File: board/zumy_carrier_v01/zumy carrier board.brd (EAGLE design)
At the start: 54 x 88.9 mm, 20 parts, among them J1 ODROID_POWER, J2 BATT_POWER, M1 POLOLU_STEP_DOWN, M2 ITG/MPU_MODULE, M3 POLOLU_DRV8833_MODULE, SW1 500SSP1S1M6QEA

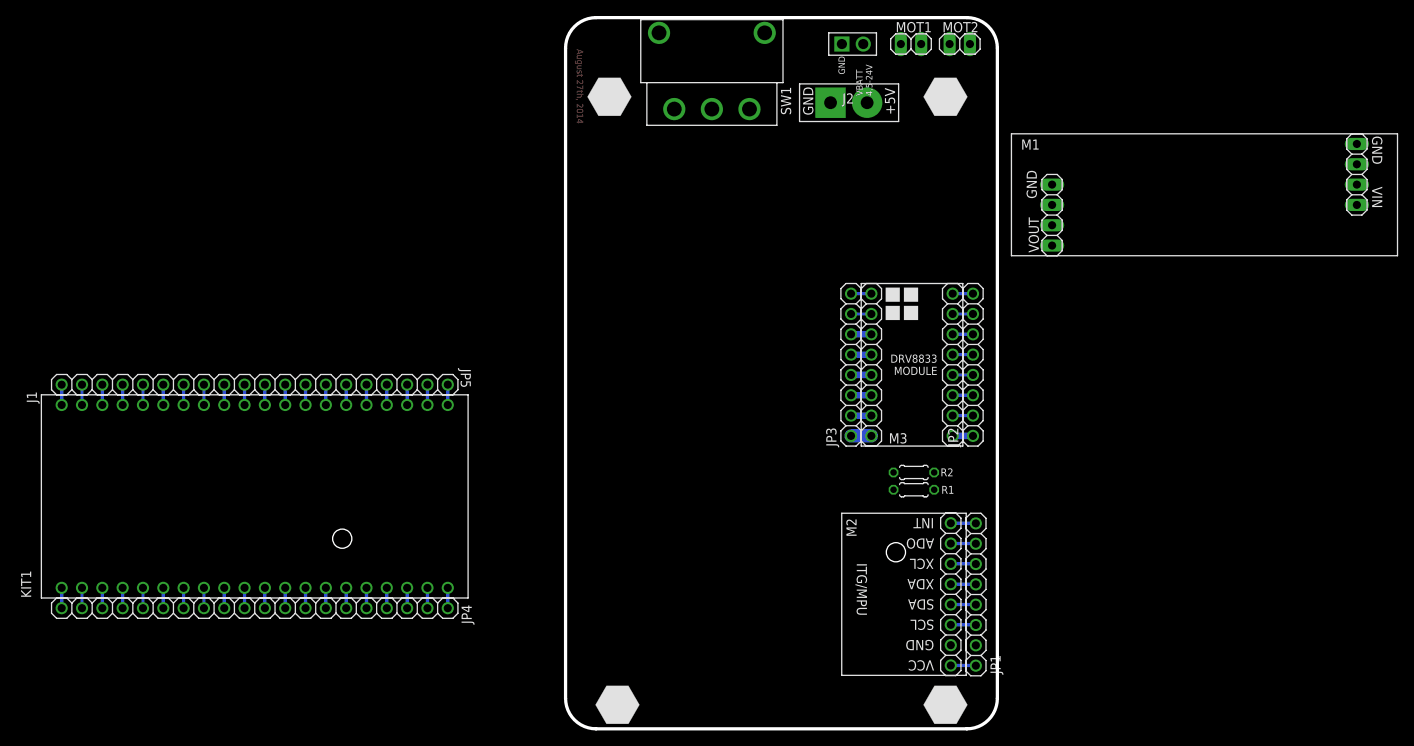
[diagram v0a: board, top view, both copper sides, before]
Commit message: Most of Rev D done. Major rearrangement. New mounting hole pattern.
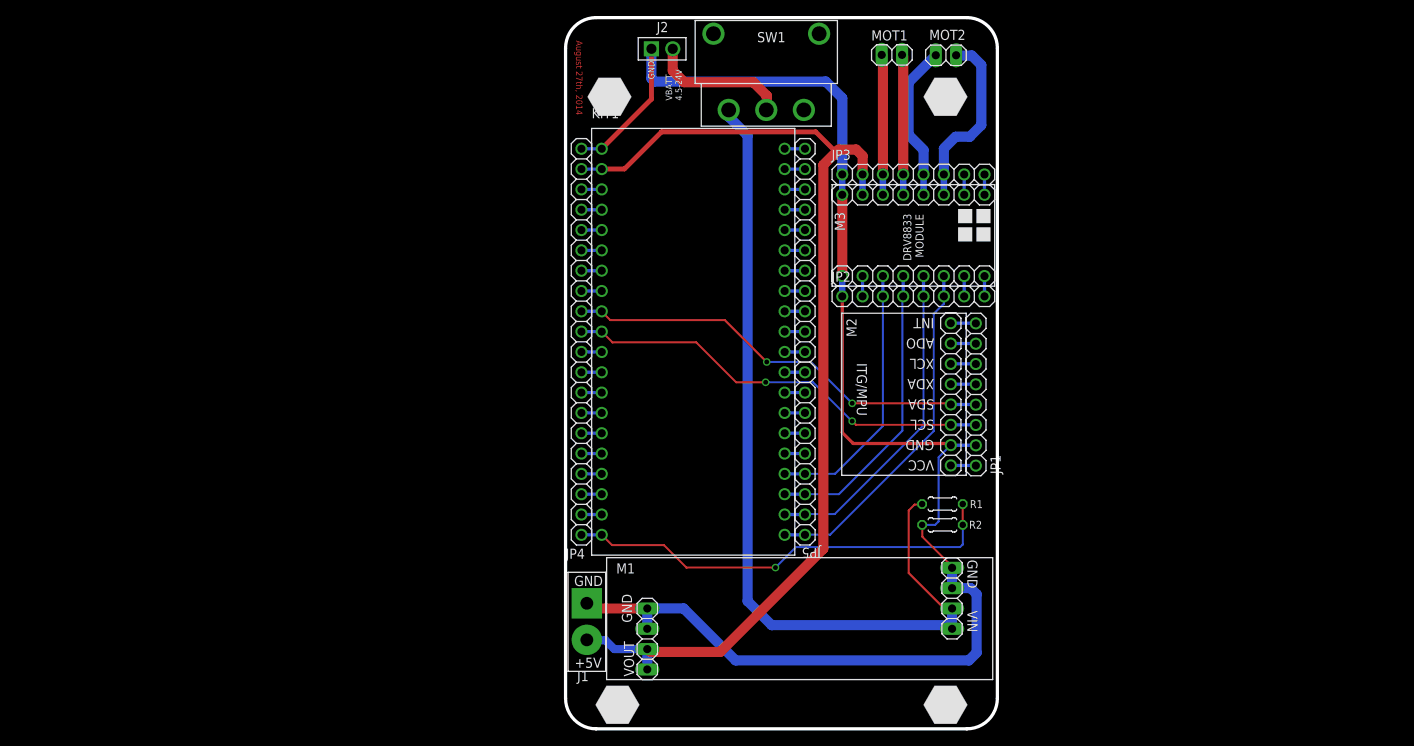
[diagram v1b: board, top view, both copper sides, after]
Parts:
- moved M1 73.3 mm to (29.3, 13.8)
- moved J1 69.6 mm to (2.66, 15.7), turned to 270 degrees
- moved JP5 69.0 mm to (29.9, 48.4), turned to 90 degrees
- moved KIT1 58.1 mm to (16.0, 48.4), turned to 0 degrees
- moved JP4 52.7 mm to (1.98, 48.4), turned to 270 degrees
- moved JP3 25.0 mm to (43.5, 69.3), turned to 0 degrees
- moved JP1 25.0 mm to (51.3, 41.8)
- moved M2 25.0 mm to (40.9, 41.8)
- moved J2 23.8 mm to (10.7, 85.0)
- moved JP2 11.3 mm to (43.5, 54.1), turned to 0 degrees
- moved R2 7.46 mm to (47.1, 25.5)
- moved SW1 6.80 mm to (25.1, 77.4)
- moved R1 3.99 mm to (47.1, 28.1)
- moved M3 3.99 mm to (53.6, 55.3), turned to 90 degrees
- moved MOT1 2.75 mm to (40.8, 84.2), turned to 0 degrees
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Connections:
- net AIN1: now also JP5.1, KIT1.P$21; no longer JP5.4, KIT1.P$24
- net AIN2: now also JP5.2, KIT1.P$22; no longer JP5.3, KIT1.P$23
- net BIN1: now also JP5.4, KIT1.P$24; no longer JP5.1, KIT1.P$21
- net BIN2: now also JP5.3, KIT1.P$23; no longer JP5.2, KIT1.P$22
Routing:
- net GND: track 8.44 -> 192.6 mm
- net +5V: track 5.08 -> 131.7 mm
- net SW_VBATT: track 0.00 -> 109.0 mm
- net V_BATT_SENSE: track 2.54 -> 55.6 mm, vias 0 -> 1
- net MPU_SDA: track 5.87 -> 54.3 mm, vias 0 -> 2
- net MPU_SCL: track 5.87 -> 54.3 mm, vias 0 -> 2
- net AIN1: track 5.08 -> 44.4 mm
- net AIN2: track 5.08 -> 40.6 mm
- net BIN2: track 5.08 -> 37.4 mm
- net BIN1: track 5.08 -> 33.5 mm
- net N$62: track 2.54 -> 22.9 mm
- net VBATT: track 0.00 -> 17.6 mm
- net N$61: track 2.54 -> 19.6 mm
- net N$60: track 2.54 -> 17.5 mm
- net N$59: track 2.54 -> 17.5 mm

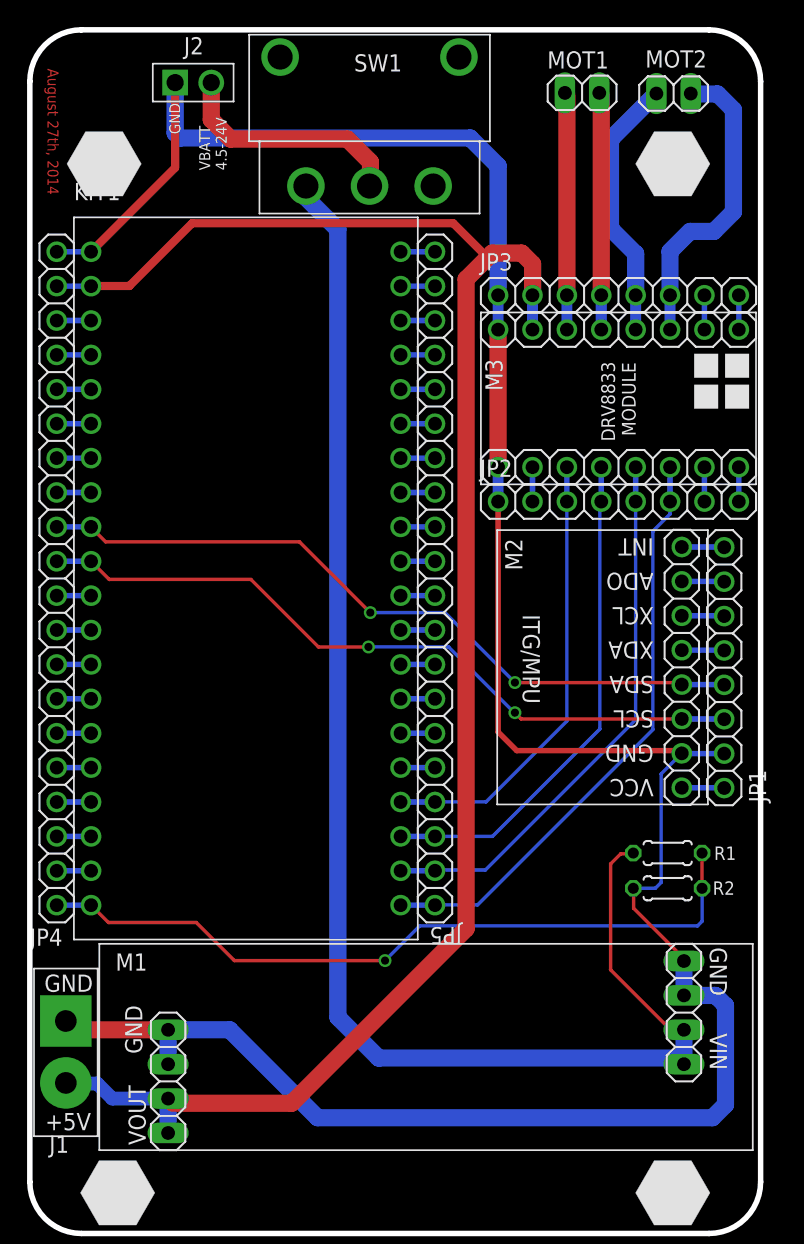
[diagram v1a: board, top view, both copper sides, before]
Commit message: Rev D done. Some library parts updated to suit new layout.
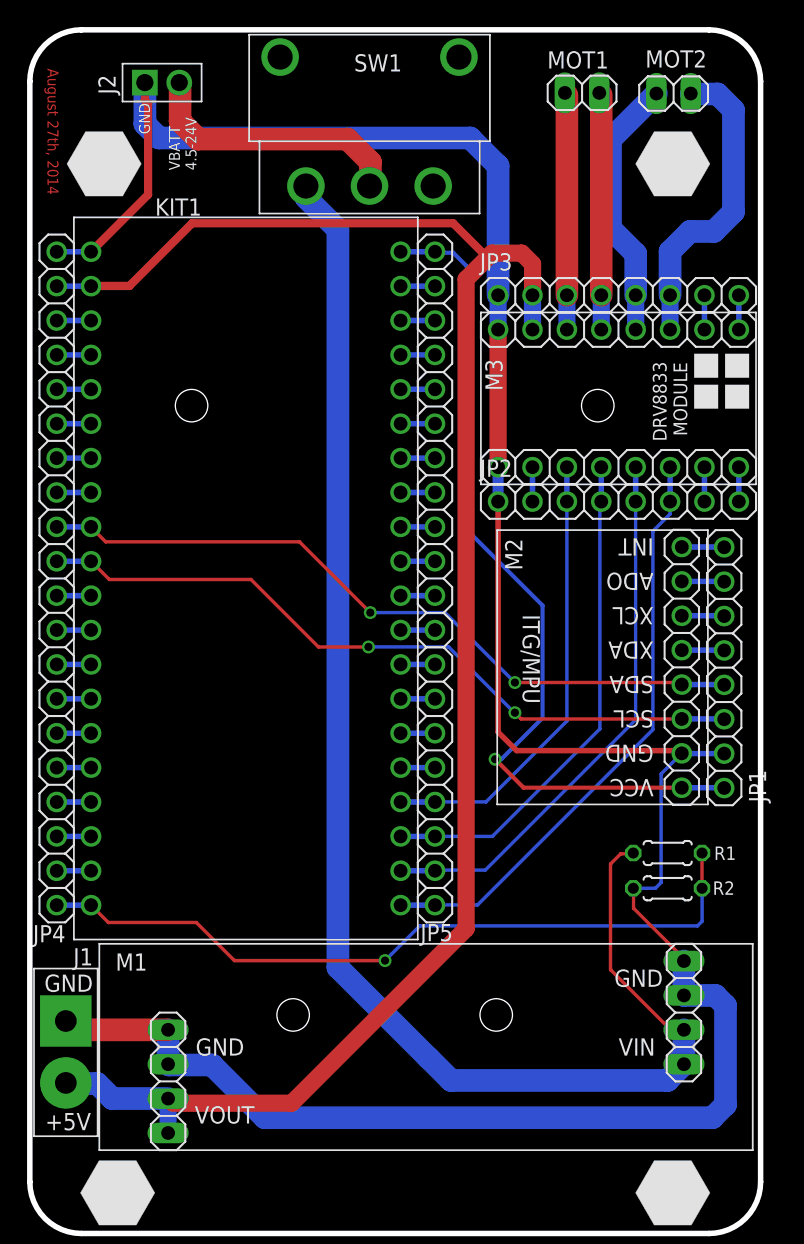
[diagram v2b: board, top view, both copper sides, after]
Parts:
- moved J2 2.24 mm to (8.50, 85.0)
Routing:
- net +3V3: track 5.69 -> 63.6 mm, vias 0 -> 1
- net VBATT: track 17.6 -> 20.0 mm
- net SW_VBATT: track 109.0 -> 108.5 mm
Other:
- board text added: "A. Pullin A.J. Chen 2014"
- board text removed: "A.J. Chen / A. Pullin 2014"

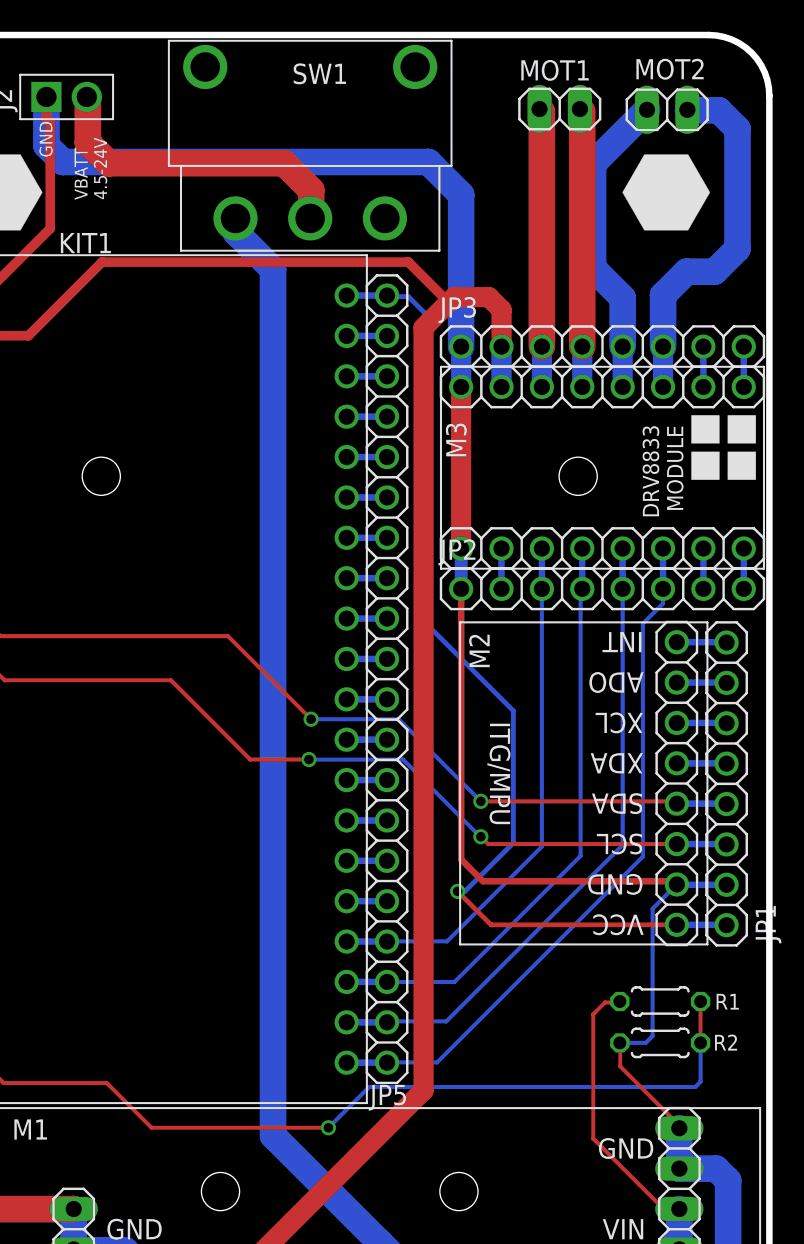
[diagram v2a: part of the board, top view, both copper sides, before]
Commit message: Minor adjustments to placement.
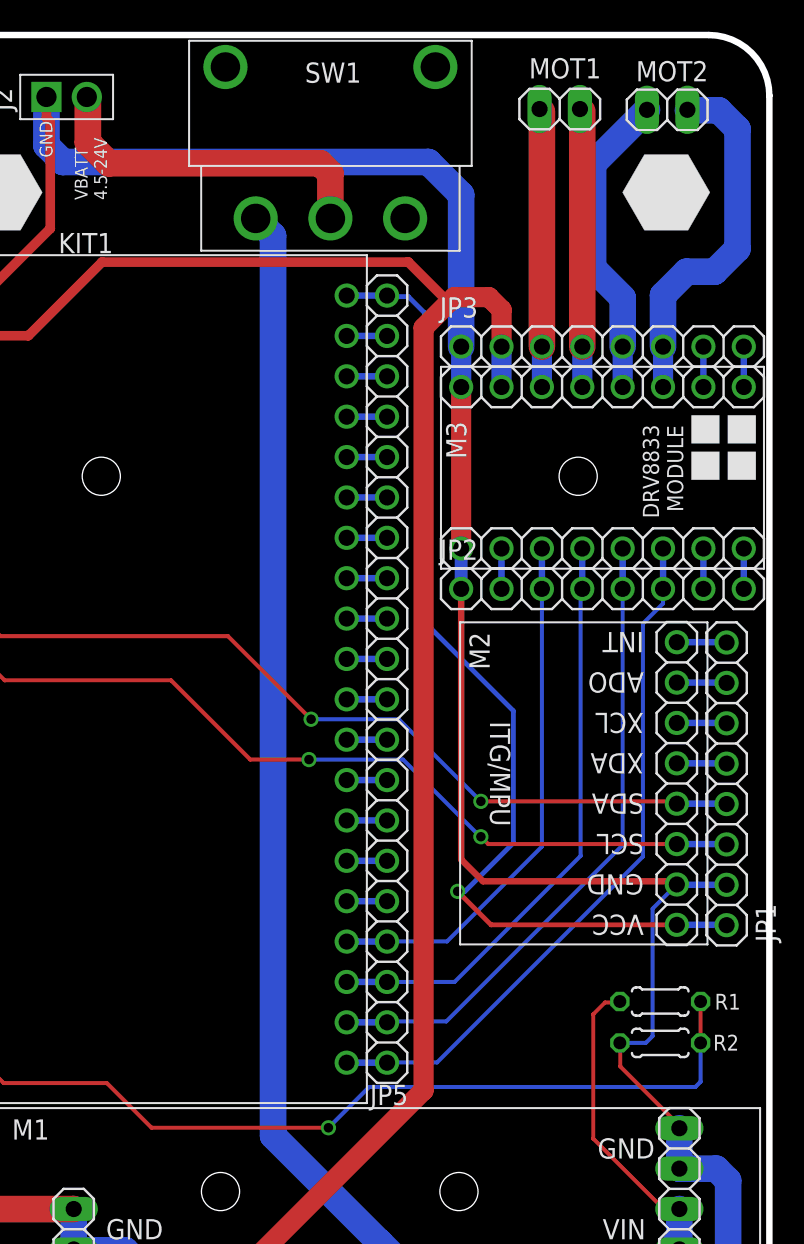
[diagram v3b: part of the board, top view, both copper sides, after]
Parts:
- moved SW1 1.27 mm to (26.4, 77.4)
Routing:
- net VBATT: track 20.0 -> 21.8 mm
- net SW_VBATT: track 108.5 -> 107.9 mm
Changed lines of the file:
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@@
 <setting verticaltext="up"/>
 </settings>
-<grid distance="1" unitdist="mil" unit="mil" style="lines" multiple="1" display="no" altdistance="0.25" altunitdist="mil" altunit="mil"/>
+<grid distance="5" unitdist="mil" unit="mil" style="lines" multiple="1" display="no" altdistance="1" altunitdist="mil" altunit="mil"/>
 <layers>
 <layer number="1" name="Top" color="4" fill="1" visible="yes" active="yes"/>
@@
 <wire x1="53.975" y1="3.81" x2="50.165" y2="0" width="0.4064" layer="20" curve="-90"/>
 <wire x1="50.165" y1="0" x2="3.81" y2="0" width="0.4064" layer="20"/>
-<text x="27.686" y="3.175" size="1.778" layer="51" font="vector" ratio="15" rot="SR180">Zumy v0.1</text>
-<text x="27.432" y="4.572" size="0.8128" layer="51" font="vector" ratio="10" rot="SR180">Biomimetic Millisystems Lab</text>
+<text x="29.083" y="3.302" size="1.9304" layer="51" font="vector" ratio="15" rot="SR180">Zumy v0.1</text>
+<text x="29.083" y="5.08" size="0.8128" layer="51" font="vector" ratio="10" rot="SR180">Biomimetic Millisystems Lab</text>
 <text x="36.909375" y="3.175" size="1.016" layer="51" font="vector" ratio="10" rot="SR180" align="center">A. Pullin
 A.J. Chen
 2014</text>
-<text x="13.462" y="2.921" size="0.8128" layer="51" font="vector" ratio="12" rot="SR180">Rev D</text>
+<text x="13.716" y="3.175" size="0.8128" layer="51" font="vector" ratio="12" rot="SR180">Rev D</text>
 <text x="1.30301875" y="86.045040625" size="0.8128" layer="1" font="vector" ratio="15" rot="SR270">August 27th, 2014</text>
 <text x="4.137025" y="6.8532375" size="0.6096" layer="48" font="vector" ratio="12" rot="R180">ODROID
 Pwr</text>
-<text x="36.123878125" y="83.030059375" size="1.6764" layer="48" font="vector" ratio="18" rot="R90">OFF</text>
+<text x="37.266878125" y="82.649059375" size="1.6764" layer="48" font="vector" ratio="18" rot="R90">OFF</text>
 <rectangle x1="16.234865625" y1="31.181603125" x2="16.742865625" y2="31.211571875" layer="52" rot="R90"/>
 <rectangle x1="15.383459375" y1="31.107940625" x2="17.654215625" y2="31.137909375" layer="52" rot="R90"/>
@@
 <rectangle x1="35.778134375" y1="84.192671875" x2="40.708271875" y2="84.222640625" layer="52" rot="R90"/>
 <text x="13.585825" y="87.3458375" size="0.8128" layer="48" font="vector" ratio="12" align="center-right">BATT</text>
-<text x="15.61496875" y="83.659346875" size="1.6764" layer="48" font="vector" ratio="18" rot="R90">ON</text>
+<text x="16.88496875" y="83.532346875" size="1.6764" layer="48" font="vector" ratio="18" rot="R90">ON</text>
 <hole x="19.447409375" y="16.1424" drill="2.4"/>
 <hole x="34.447409375" y="16.1424" drill="2.4"/>
@@
 </element>
 <element name="MOT1" library="pinhead" package="1X02" value="" x="40.788284375" y="84.243228125" smashed="yes">
-<attribute name="NAME" x="38.2152625" y="86.041546875" size="1.27" layer="25" ratio="10"/>
+<attribute name="NAME" x="38.8502625" y="86.168546875" size="1.27" layer="25" ratio="10"/>
 <attribute name="VALUE" x="38.248284375" y="81.068228125" size="1.27" layer="27"/>
 </element>
 <element name="MOT2" library="pinhead" package="1X02" value="" x="47.547528125" y="84.194965625" smashed="yes" rot="R180">
-<attribute name="NAME" x="49.998628125" y="87.382665625" size="1.27" layer="25" ratio="10" rot="R180"/>
+<attribute name="NAME" x="50.125628125" y="87.255665625" size="1.27" layer="25" ratio="10" rot="R180"/>
 <attribute name="VALUE" x="50.087528125" y="87.369965625" size="1.27" layer="27" rot="R180"/>
 </element>
@@
 <attribute name="VALUE" x="8.0438625" y="18.5626375" size="1.27" layer="27" ratio="10" rot="R270"/>
 </element>
-<element name="SW1" library="zumy" package="500SSP1S1M6QEA_SWITCH" value="500SSP1S1M6QEA" x="25.090121875" y="77.36331875" smashed="yes">
-<attribute name="NAME" x="27.487884375" y="87.09310625" size="1.27" layer="25" rot="R180"/>
+<element name="SW1" library="zumy" package="500SSP1S1M6QEA_SWITCH" value="500SSP1S1M6QEA" x="26.360121875" y="77.36331875" smashed="yes">
+<attribute name="NAME" x="28.300684375" y="87.16930625" size="1.27" layer="25" rot="R180"/>
 </element>
 <element name="J2" library="zumy" package="BATT_POWER" value="BATT_POWER" x="8.4963" y="85.0026875" smashed="yes">
@@
 <contactref element="SW1" pad="2"/>
 <contactref element="J2" pad="PWR"/>
-<wire x1="12.41298125" y1="80.83041875" x2="23.464521875" y2="80.83041875" width="1.6764" layer="1"/>
-<wire x1="23.464521875" y1="80.83041875" x2="25.156159375" y2="79.13878125" width="1.6764" layer="1"/>
-<wire x1="25.156159375" y1="79.13878125" x2="25.156159375" y2="77.42935625" width="1.6764" layer="1"/>
-<wire x1="25.156159375" y1="77.42935625" x2="25.090121875" y2="77.36331875" width="1.27" layer="1"/>
+<wire x1="12.41298125" y1="80.83041875" x2="25.72258125" y2="80.83041875" width="1.6764" layer="1"/>
 <wire x1="12.41298125" y1="80.83041875" x2="11.0998" y2="82.1436" width="1.6764" layer="1"/>
 <wire x1="11.0998" y1="82.1436" x2="11.0998" y2="84.9391875" width="1.6764" layer="1"/>
 <wire x1="11.0998" y1="84.9391875" x2="11.0363" y2="85.0026875" width="1.6764" layer="1"/>
+<wire x1="25.72258125" y1="80.83041875" x2="26.360121875" y2="80.192878125" width="1.6764" layer="1"/>
+<wire x1="26.360121875" y1="77.36331875" x2="26.360121875" y2="80.192878125" width="1.6764" layer="1"/>
 </signal>
 <signal name="+5V">
@@
 <contactref element="R1" pad="2"/>
 <wire x1="48.31225" y1="12.504" x2="48.31225" y2="15.044" width="1.6764" layer="16"/>
-<wire x1="20.391121875" y1="77.36331875" x2="20.391121875" y2="76.51495625" width="1.6764" layer="16"/>
-<wire x1="20.391121875" y1="76.51495625" x2="22.75331875" y2="74.152759375" width="1.6764" layer="16"/>
-<wire x1="22.75331875" y1="74.152759375" x2="22.75331875" y2="19.65198125" width="1.6764" layer="16"/>
+<wire x1="22.75331875" y1="76.271121875" x2="22.75331875" y2="19.65198125" width="1.6764" layer="16"/>
 <wire x1="22.75331875" y1="19.65198125" x2="29.448759375" y2="12.956540625" width="1.6764" layer="16"/>
 <wire x1="47.859709375" y1="12.956540625" x2="48.31225" y2="12.504" width="1.27" layer="16"/>
@@
 <wire x1="31.115" y1="11.303" x2="47.11125" y2="11.303" width="1.6764" layer="16"/>
 <wire x1="47.11125" y1="11.303" x2="48.31225" y2="12.504" width="1.6764" layer="16"/>
+<wire x1="22.75331875" y1="76.271121875" x2="21.661121875" y2="77.36331875" width="1.6764" layer="16"/>
 </signal>
 </signals>
